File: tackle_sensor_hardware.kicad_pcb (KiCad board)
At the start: 4 copper layers, 45.1 x 57.2 mm, 74 parts, among them J1 Conn_01x02_Male, J2 Conn_01x04_Male, J3 Conn_01x03_Male, J4 Conn_ARM_JTAG_SWD_10, Q1 DMP4051LK3, Q9 NCE0110K, SW1 PTS645SL43SMTR92 LFS, SW2 SW_DPDT_x2, T1 DRQ125-330-R, U1 LIS2DE12, U2 STM32G031Fx, U3 LM3488, U4 LD1117S33TR_SOT223, U5 ULN2003ADR

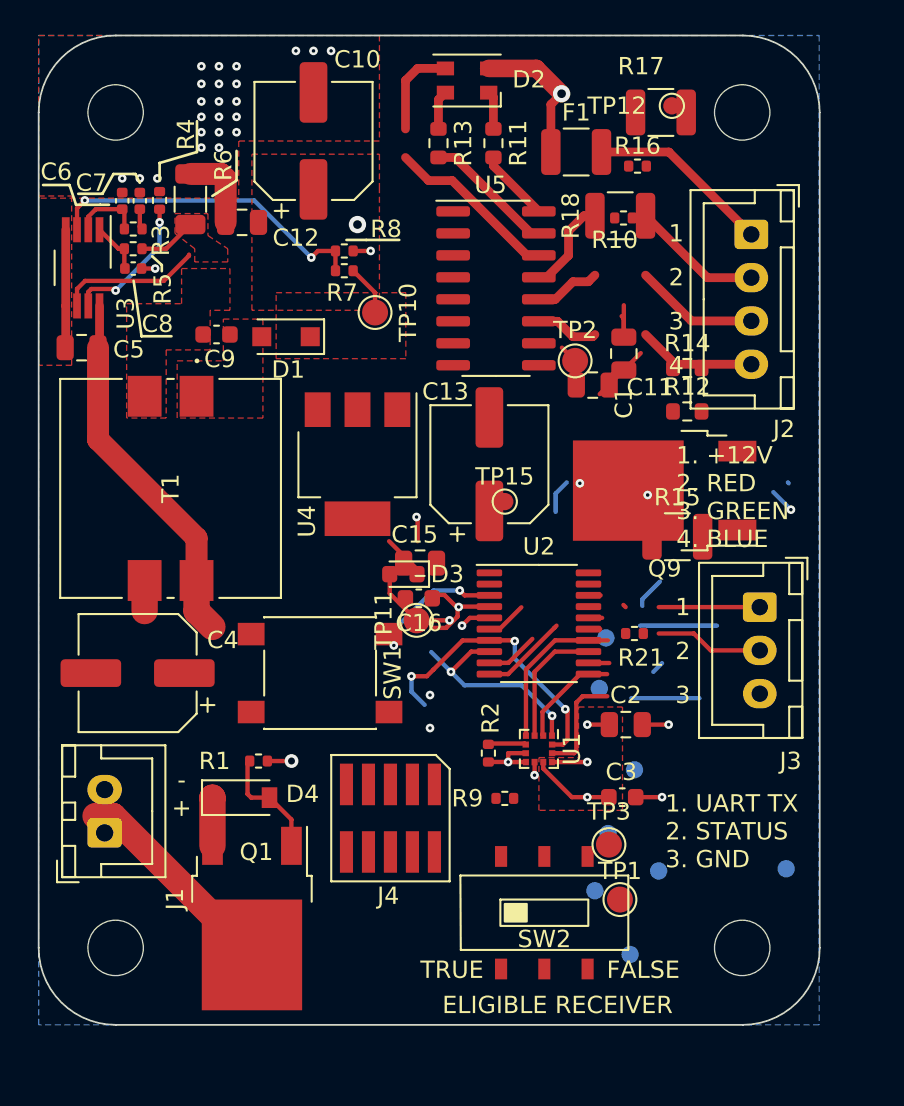
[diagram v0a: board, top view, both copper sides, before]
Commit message: rerouted PCB after changes
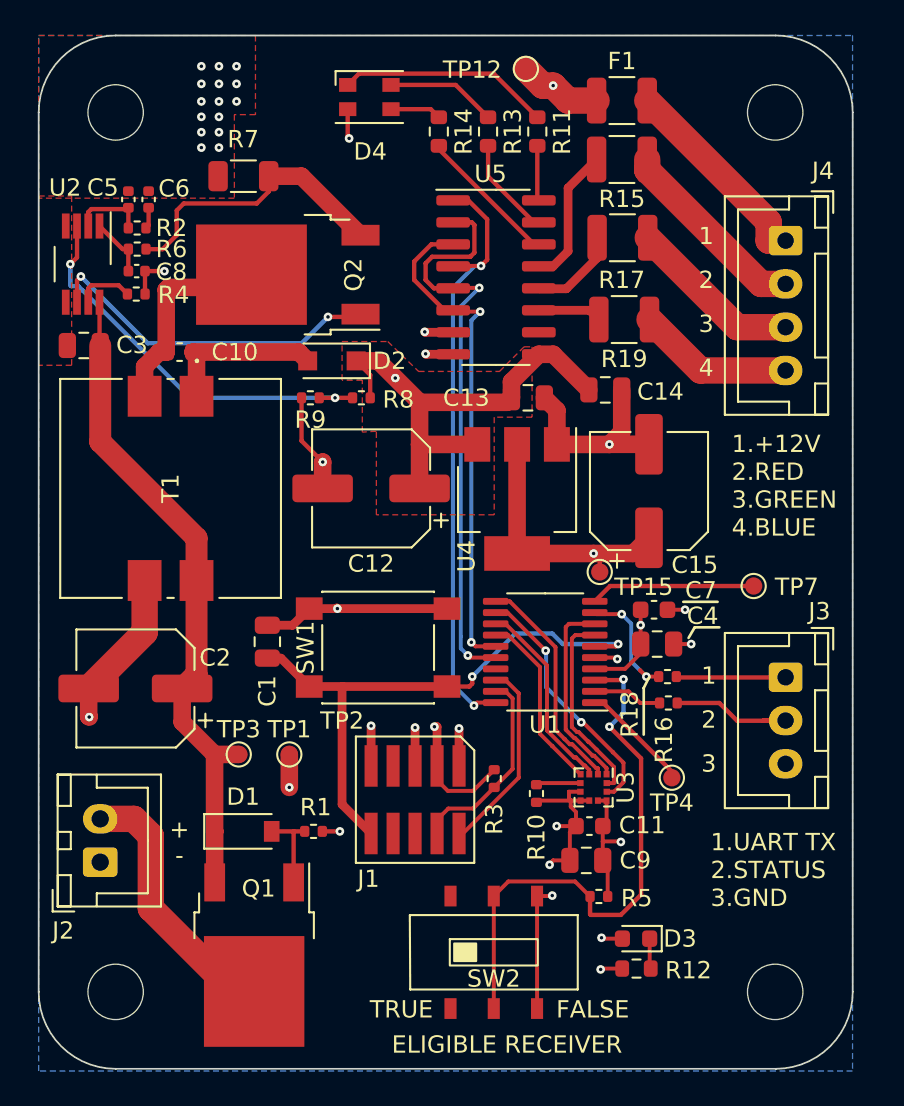
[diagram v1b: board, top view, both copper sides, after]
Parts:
- removed C16: 1uF, 50V, Capacitor_SMD:C_0603_1608Metric
- removed Q9: NCE0110K, Package_TO_SOT_SMD:TO-252-2
- removed R21: 220,1%,63mW, Resistor_SMD:R_0402_1005Metric
- removed TP5: TestPoint, TestPoint:TestPoint_Pad_D1.0mm
- added C14: 100nF, 50V, Capacitor_SMD:C_0805_2012Metric, F.Cu at (153.4, 90.3)
- added Q2: NCE0110K, Package_TO_SOT_SMD:TO-252-2, F.Cu at (135.0, 83.7)
- added R19: 0,0.5W, Resistor_SMD:R_1210_3225Metric, F.Cu at (154.5, 86.3)
- C10: value 22uF, 20V -> 1uF, 50V; footprint Capacitor_SMD:CP_Elec_6.3x5.9 -> Capacitor_SMD:C_0603_1608Metric
- C11: value 100nF, 50V -> 1uF, 50V; footprint Capacitor_SMD:C_0805_2012Metric -> Capacitor_SMD:C_0603_1608Metric
- C12: value 100nF, 50V -> 22uF, 20V; footprint Capacitor_SMD:C_0805_2012Metric -> Capacitor_SMD:CP_Elec_6.3x5.9
- C13, C4: value 10uF, 50V -> 100nF, 50V; footprint Capacitor_SMD:CP_Elec_6.3x5.8 -> Capacitor_SMD:C_0805_2012Metric
- C15, C2: value 100nF, 50V -> 10uF, 50V; footprint Capacitor_SMD:C_0805_2012Metric -> Capacitor_SMD:CP_Elec_6.3x5.8
- C3: value 10u -> 100nF, 50V; footprint Capacitor_SMD:C_0603_1608Metric -> Capacitor_SMD:C_0805_2012Metric
- C5: value 100nF, 50V -> 2200pF,10%,50V; footprint Capacitor_SMD:C_0805_2012Metric -> Capacitor_SMD:C_0402_1005Metric
- C6: value 2200pF,10%,50V -> 0.22uF,10%,35V
- C7: value 0.22uF,10%,35V -> 1uF, 50V; footprint Capacitor_SMD:C_0402_1005Metric -> Capacitor_SMD:C_0603_1608Metric
- C9: value 1uF, 50V -> 100nF, 50V; footprint Capacitor_SMD:C_0603_1608Metric -> Capacitor_SMD:C_0805_2012Metric
- D1: value DSK34 -> BZT52-B15_R1_00001; footprint Diode_SMD:D_SOD-123F -> Diode_SMD:D_SOD-123
- D2: value CLV1A-FKB-CK1VW1DE1BB7C3C3 -> DSK34; footprint LED_SMD:LED_Cree-PLCC4_3.2x2.8mm_CCW -> Diode_SMD:D_SOD-123F
- D4: value BZT52-B15_R1_00001 -> CLV1A-FKB-CK1VW1DE1BB7C3C3; footprint Diode_SMD:D_SOD-123 -> LED_SMD:LED_Cree-PLCC4_3.2x2.8mm_CCW
- J1: value Conn_01x02_Male -> Conn_ARM_JTAG_SWD_10; footprint Connector_JST:JST_XH_B2B-XH-A_1x02_P2.50mm_Vertical -> rfc_footprint_lib:20021121-00010C4LF
- J2: value Conn_01x04_Male -> Conn_01x02_Male; footprint Connector_JST:JST_XH_B4B-XH-A_1x04_P2.50mm_Vertical -> Connector_JST:JST_XH_B2B-XH-A_1x02_P2.50mm_Vertical
- J4: value Conn_ARM_JTAG_SWD_10 -> Conn_01x04_Male; footprint rfc_footprint_lib:20021121-00010C4LF -> Connector_JST:JST_XH_B4B-XH-A_1x04_P2.50mm_Vertical
- R10: value 10k,1%,63mW -> 0,63mW
- R18: value 0,0.5W -> 220,1%,63mW; footprint Resistor_SMD:R_1210_3225Metric -> Resistor_SMD:R_0402_1005Metric
- R2: value 0,63mW -> 634,.1%,63mW
- R3: value 634,.1%,0.1W -> 10k,1%,63mW
- R5: value 100,1%,63mW -> 10k,1%,63mW
- R6: value 25mOhm,1%,500mW -> 100,1%,63mW; footprint Resistor_SMD:R_1206_3216Metric -> Resistor_SMD:R_0402_1005Metric
- R7: value 84.5k,1%,63mW -> 25mOhm,1%,500mW; footprint Resistor_SMD:R_0402_1005Metric -> Resistor_SMD:R_1206_3216Metric
- R8: value 10k,1%,63mW -> 84.5k,1%,63mW
- TP1, TP3: footprint TestPoint:TestPoint_Pad_D1.5mm -> TestPoint:TestPoint_Pad_D1.0mm
- TP10, TP11, TP2: footprint TestPoint:TestPoint_Pad_D1.5mm -> rfc_footprint_lib:test_point
- TP13, TP14, TP6, TP8, TP9: footprint TestPoint:TestPoint_Pad_D1.0mm -> rfc_footprint_lib:test_point; moved to F.Cu
- TP4, TP7: moved to F.Cu
- U1: value LIS2DE12 -> STM32G031Fx; footprint Package_LGA:LGA-12_2x2mm_P0.5mm -> Package_SO:TSSOP-20_4.4x6.5mm_P0.65mm
- U2: value STM32G031Fx -> LM3488; footprint Package_SO:TSSOP-20_4.4x6.5mm_P0.65mm -> Package_SO:VSSOP-8_3.0x3.0mm_P0.65mm
- U3: value LM3488 -> LIS2DE12; footprint Package_SO:VSSOP-8_3.0x3.0mm_P0.65mm -> Package_LGA:LGA-12_2x2mm_P0.5mm
- moved J2 52.2 mm to (124.2, 117.6), turned to 90 degrees
- moved R5 46.1 mm to (153.0, 119.6), turned to 180 degrees
- moved U3 42.1 mm to (152.7, 113.3)
- moved D4 41.1 mm to (139.8, 73.4)
- moved C3 40.6 mm to (123.3, 87.8), turned to 180 degrees
- moved J4 40.4 mm to (163.8, 81.7), turned to -90 degrees
- moved R3 38.0 mm to (147.0, 112.8), turned to -90 degrees
- moved C7 38.0 mm to (156.2, 103.0), turned to 0 degrees
- moved C9 37.1 mm to (152.3, 117.5)
- moved R2 36.5 mm to (126.3, 81.0), turned to 0 degrees
- moved R10 33.6 mm to (149.4, 113.6), turned to -90 degrees
- moved U2 33.5 mm to (123.2, 83.1), turned to -90 degrees
- moved R12 32.3 mm to (155.2, 123.7), turned to 180 degrees
- moved R16 31.1 mm to (157.0, 108.4)
- moved C4 30.1 mm to (156.4, 105.0), turned to 0 degrees
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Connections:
- C10 pad 1: +12V -> Net-(C10-Pad1)
- C10 pad 2: GND -> Net-(C10-Pad2)
- C11 pad 1: +12V -> +3V3
- C13 pad 1: +3V3 -> +12V
- C2 pad 1: +3V3 -> Net-(C2-Pad1)
- C3 pad 1: +3V3 -> Net-(C2-Pad1)
- C4 pad 1: Net-(C4-Pad1) -> +3V3
- C5 pad 1: Net-(C4-Pad1) -> Net-(C5-Pad1)
- C7 pad 1: Net-(C7-Pad1) -> +3V3
- C9 pad 1: Net-(C9-Pad1) -> +3V3
- C9 pad 2: Net-(C9-Pad2) -> GND
- D1 pad 1: +12V -> Net-(C2-Pad1)
- D1 pad 2: Net-(C9-Pad1) -> Net-(D1-Pad2)
- D2 pad 1: Net-(D2-Pad1) -> +12V
- D2 pad 2: +12V -> Net-(C10-Pad1)
- D4 pad 1: Net-(C4-Pad1) -> Net-(D4-Pad1)
- D4 pad 2: Net-(D4-Pad2) -> +12V
- J1 pad 1: GND -> +3V3
- J1 pad 2: Net-(J1-Pad2) -> /SWDIO
- J2 pad 1: Net-(F1-Pad2) -> GND
- J4 pad 1: +3V3 -> Net-(F1-Pad2)
- J4 pad 2: /SWDIO -> Net-(J4-Pad2)
- J4 pad 3: GND -> Net-(J4-Pad3)
- J4 pad 4: /SWCLK -> Net-(J4-Pad4)
- Q1 pad 1: Net-(D4-Pad2) -> Net-(D1-Pad2)
- Q1 pad 2: Net-(J1-Pad2) -> Net-(J2-Pad2)
- Q1 pad 3: Net-(C4-Pad1) -> Net-(C2-Pad1)
- R1 pad 1: Net-(D4-Pad2) -> Net-(D1-Pad2)
- R10 pad 1: Net-(R7-Pad2) -> Net-(R10-Pad1)
- R11 pad 1: Net-(D2-Pad1) -> Net-(D4-Pad1)
- R12 pad 1: Net-(D2-Pad4) -> Net-(D3-Pad1)
- R12 pad 2: Net-(U5-Pad15) -> GND
- R13 pad 1: Net-(D2-Pad3) -> Net-(D4-Pad4)
- R13 pad 2: Net-(U5-Pad14) -> Net-(R13-Pad2)
- R14 pad 1: Net-(D3-Pad1) -> Net-(D4-Pad3)
- R14 pad 2: GND -> Net-(R14-Pad2)
- R15 pad 1: Net-(U5-Pad12) -> Net-(J4-Pad2)
- R15 pad 2: Net-(J2-Pad3) -> Net-(R15-Pad2)
- R16 pad 1: UART_TX -> TACKLE_STATUS
- R16 pad 2: Net-(J3-Pad1) -> Net-(J3-Pad2)
- R17 pad 1: Net-(U5-Pad11) -> Net-(J4-Pad3)
- R17 pad 2: Net-(J2-Pad4) -> Net-(R17-Pad2)
- R18 pad 1: Net-(R18-Pad1) -> UART_TX
- R18 pad 2: Net-(J2-Pad2) -> Net-(J3-Pad1)
- R2 pad 1: Net-(R2-Pad1) -> Net-(C5-Pad1)
- R2 pad 2: GND -> Net-(C6-Pad1)
- R3 pad 1: Net-(C6-Pad1) -> GND
- R3 pad 2: Net-(C7-Pad1) -> /SWCLK
- R5 pad 1: Net-(C8-Pad1) -> +3V3
- R5 pad 2: Net-(Q9-Pad2) -> Net-(R5-Pad2)
- R6 pad 1: Net-(Q9-Pad2) -> Net-(C8-Pad1)
- R6 pad 2: GND -> Net-(Q2-Pad2)
- R7 pad 1: +12V -> Net-(Q2-Pad2)
- R7 pad 2: Net-(R7-Pad2) -> GND
- R8 pad 1: GND -> +12V
- R8 pad 2: /SWCLK -> Net-(R8-Pad2)
- R9 pad 1: +3V3 -> Net-(R8-Pad2)
- R9 pad 2: Net-(SW2-Pad2) -> GND
- SW2 pad 2: Net-(SW2-Pad2) -> Net-(R5-Pad2)
- SW2 pad 5: Net-(SW2-Pad2) -> Net-(R5-Pad2)
- T1 pad 1: Net-(C9-Pad1) -> Net-(C10-Pad1)
- T1 pad 2: Net-(C9-Pad2) -> Net-(C10-Pad2)
- T1 pad 4: Net-(C4-Pad1) -> Net-(C2-Pad1)
- TP10 pad 1: +12V -> /SPI1_MISO
- TP11 pad 1: +3V3 -> /SPI1_SCK
- TP12 pad 1: Net-(TP12-Pad1) -> +12V
- TP13 pad 1: UART_TX -> /ACC_INT1
- TP14 pad 1: UART_RX -> /ACC_INT2
- TP15 pad 1: Net-(TP15-Pad1) -> +3V3
- TP3 pad 1: Net-(C4-Pad1) -> Net-(C2-Pad1)
- TP4 pad 1: /SPI1_NSS -> Net-(TP4-Pad1)
- TP6 pad 1: /SPI1_MISO -> UART_TX
- TP7 pad 1: /SPI1_SCK -> UART_RX
- TP8 pad 1: /ACC_INT1 -> /SPI1_NSS
- TP9 pad 1: /ACC_INT2 -> /SPI1_MOSI
- U1 pad 1: /SPI1_SCK -> Net-(TP4-Pad1)
- U1 pad 10: +3V3 -> UART_RX
- U1 pad 11: /ACC_INT2 -> /SPI1_NSS
- U1 pad 12: /ACC_INT1 -> /ACC_INT2
- U1 pad 2: /SPI1_NSS -> TACKLE_STATUS
- U1 pad 3: /SPI1_MISO -> Net-(R5-Pad2)
- U1 pad 4: /SPI1_MOSI -> +3V3
- U1 pad 5: Net-(R2-Pad1) -> GND
- U1 pad 6: GND -> /RST
- U1 pad 7: GND -> /ACC_INT1
- U1 pad 8: GND -> /SPI1_SCK
- U1 pad 9: +3V3 -> UART_TX
- U2 pad 1: Net-(TP15-Pad1) -> Net-(C8-Pad1)
- U2 pad 2: TACKLE_STATUS -> Net-(C5-Pad1)
- U2 pad 3: Net-(SW2-Pad2) -> Net-(R8-Pad2)
- U2 pad 4: +3V3 -> GND
- U2 pad 6: /RST -> Net-(Q2-Pad1)
- U2 pad 7: /ACC_INT1 -> Net-(R4-Pad1)
- U2 pad 8: /SPI1_SCK -> Net-(C2-Pad1)
- U3 pad 1: Net-(C8-Pad1) -> /SPI1_SCK
- U3 pad 2: Net-(C6-Pad1) -> /SPI1_NSS
- U3 pad 3: Net-(R7-Pad2) -> /SPI1_MISO
- U3 pad 4: GND -> /SPI1_MOSI
- U3 pad 5: GND -> Net-(R10-Pad1)
- U3 pad 6: Net-(Q9-Pad1) -> GND
- U3 pad 7: Net-(R4-Pad1) -> GND
- U3 pad 8: Net-(C4-Pad1) -> GND
- U5 pad 11: Net-(U5-Pad11) -> Net-(R19-Pad2)
- U5 pad 12: Net-(U5-Pad12) -> Net-(R17-Pad2)
- U5 pad 13: Net-(R18-Pad1) -> Net-(R15-Pad2)
- U5 pad 14: Net-(U5-Pad14) -> Net-(R14-Pad2)
- U5 pad 15: Net-(U5-Pad15) -> Net-(R13-Pad2)
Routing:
- net +12V: track 11.4 -> 63.8 mm, vias 2 -> 3
- net GND: track 29.4 -> 80.9 mm, vias 32 -> 34
- net Net-(C2-Pad1): track 0.00 -> 38.5 mm
- net R_PWM: track 0.00 -> 36.0 mm, vias 0 -> 2
- net G_PWM: track 0.79 -> 33.7 mm, vias 0 -> 2
- net Net-(R5-Pad2): track 0.00 -> 32.5 mm, vias 0 -> 2
- net B_PWM: track 0.67 -> 29.1 mm, vias 0 -> 2
- net /RST: track 6.80 -> 33.3 mm, vias 0 -> 2
- net Net-(C4-Pad1): track 24.2 -> 0.00 mm
- net Net-(R8-Pad2): track 0.00 -> 23.5 mm, vias 0 -> 2
- net Net-(Q2-Pad1): track 0.00 -> 20.3 mm, vias 0 -> 2
- net Net-(R7-Pad2): track 19.0 -> 0.00 mm, vias 2 -> 0
- net Net-(Q2-Pad2): track 0.00 -> 16.9 mm
- net Net-(C10-Pad2): track 0.00 -> 13.0 mm
- net +3V3: track 19.1 -> 31.7 mm
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- removed copper zone on F.Cu, net +3V3
- removed copper zone on F.Cu, net Net-(C9-Pad1)
- removed copper zone on F.Cu, net Net-(C9-Pad2)
- removed copper zone on F.Cu, net Net-(Q9-Pad1)
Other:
- board size 45.1 x 57.2 mm -> 47 x 59.7 mm
- board text added: "1.+12V 2.RED 3.GREEN 4.BLUE"
- board text added: "1.UART TX 2.STATUS 3.GND"
- board text added: "Robotic Football Tackle Sensor V0.2 10/23/2022"
- board text removed: "1. +12V 2. RED 3. GREEN 4. BLUE"
- board text removed: "1. UART TX 2. STATUS 3. GND"
- board text removed: "Robotic Football Tackle Sensor V0.0 4/18/2022"

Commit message: adding release v0.1
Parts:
- removed the G*** at (143.4, 95.5) (x2)
- added G***: LOGO, rfc_footprint_lib:new_logo_mask, B.Cu at (145.2, 96.3)
- added G***: LOGO, rfc_footprint_lib:new_logo_silk, B.Cu at (145.2, 96.3)
- moved C10 1.27 mm to (127.5, 87.9)
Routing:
- net Net-(C10-Pad1): track 9.47 -> 11.1 mm
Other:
- board text added: "Tackle Sensor V0.1 10/24/2022"
- board text removed: "Robotic Football Tackle Sensor V0.2 10/23/2022"

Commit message: - updates for release v0.1
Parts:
- removed TP6: TestPoint, rfc_footprint_lib:test_point
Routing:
- net /SWDIO: track 11.3 -> 12.4 mm
- net R_PWM: track 36.0 -> 35.0 mm
- net Net-(C10-Pad2): track 12.8 -> 12.0 mm
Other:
- board text added: "Tackle Sensor V0.1 12/1/2022"
- board text removed: "Tackle Sensor V0.1 10/24/2022"

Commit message: - add reference PDFs and dimensions to the layout
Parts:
- moved C14 39.5 mm to (145.4, 51.6)
- moved C15 39.5 mm to (147.9, 57.4)
- moved D1 39.5 mm to (124.5, 77.1)
- moved F1 39.5 mm to (146.4, 34.9)
- moved J1 39.5 mm to (134.4, 75.3)
- moved R10 39.5 mm to (141.4, 74.9)
- moved R12 39.5 mm to (147.2, 85.0)
- moved R14 39.5 mm to (135.8, 36.7)
- moved R15 39.5 mm to (146.4, 38.3)
- moved R3 39.5 mm to (139.0, 74.0)
- moved R5 39.5 mm to (145.0, 80.8)
- moved R9 39.5 mm to (128.4, 52.0)
- moved SW1 39.5 mm to (132.3, 66.5)
- moved TP12 39.5 mm to (140.8, 33.0)
- moved TP13 39.5 mm to (144.4, 71.9)
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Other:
- board text added: "Electrical Connector Details Power Connector - J2 Pin 1 - GND Pin 2 - V+ (10V to 30V) Status Connector - J3 (Optional) Pin 1 - UART TX (115200 bps, 8N1, 3.3V Logic Output) Pin 2 - STATUS (3.3V Logic Output) Pin 3 - GND LED Connector - J4 (Common Anode RGB LED) Pin 1 - +12V Pin 2 - RED Pin 3 - GREEN Pin 4 - BLUE"

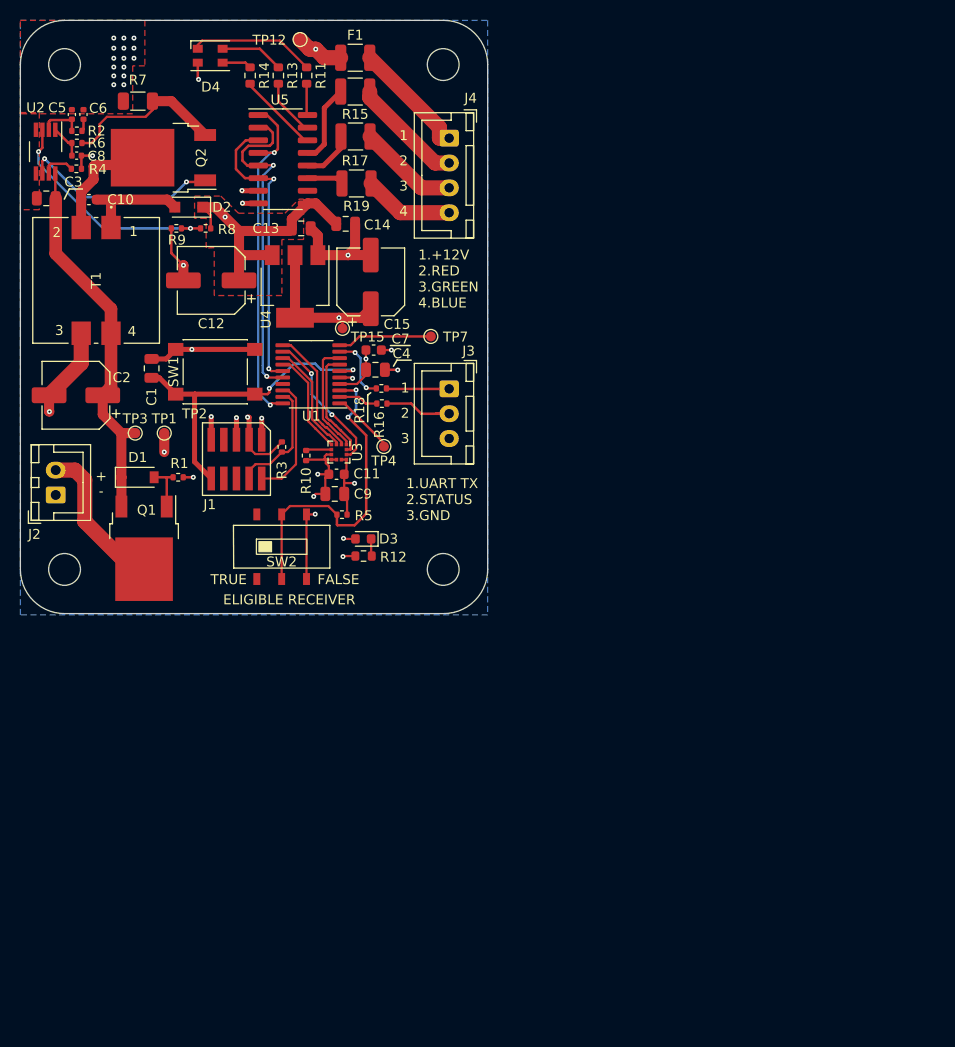
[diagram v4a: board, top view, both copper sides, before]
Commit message: - change page size to legal
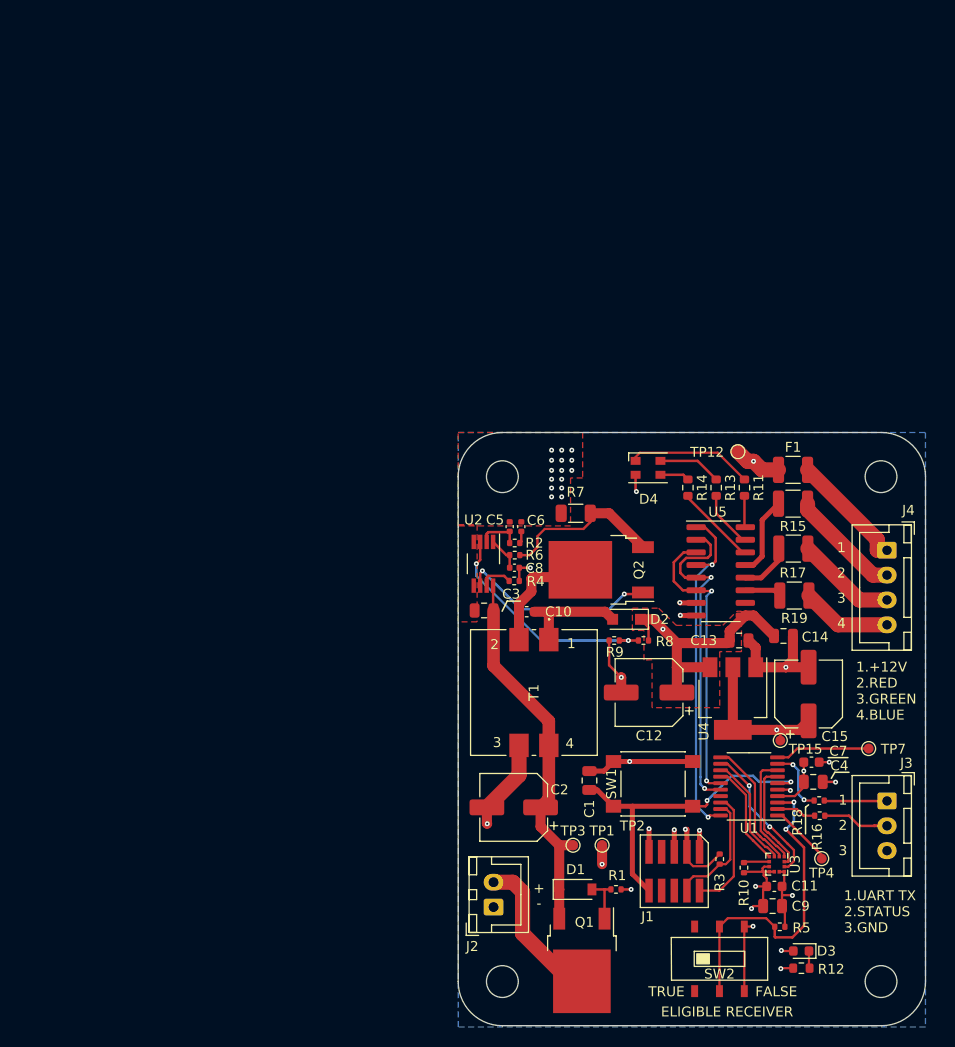
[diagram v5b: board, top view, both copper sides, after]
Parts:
- moved C15 60.5 mm to (192.0, 98.9)
- moved J1 60.5 mm to (178.5, 116.7)
- moved R14 60.5 mm to (179.8, 78.1)
- moved TP13 60.5 mm to (188.5, 113.4)
- moved C1 60.5 mm to (169.9, 107.6)
- moved C14 60.5 mm to (189.5, 93.1)
- moved H3 60.5 mm to (161.2, 127.8)
- moved R12 60.5 mm to (191.3, 126.5)
- moved R2 60.5 mm to (162.4, 83.7)
- moved R5 60.5 mm to (189.1, 122.3)
- moved R9 60.5 mm to (172.4, 93.5)
- moved SW1 60.5 mm to (176.3, 107.9)
- moved T1 60.5 mm to (164.4, 98.7)
- moved U3 60.5 mm to (188.8, 116.0)
- moved C10 60.5 mm to (163.6, 90.6)
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
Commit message: - added additional notes to the reference_sheet and the schematic sheet
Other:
- board text added: "Electrical Connector Details Power Connector - J2 Mating Connector Housing: XHP-2 Mating Connector Pins: (see below) - Pin 1 - GND - Pin 2 - V+ (10V to 30V) Status Connector - J3 (Optional) Mating Connector Housing: XHP-3 Mating Connector Pins: (see below) - Pin 1 - UART TX (115200 bps, 8N1, 3.3V Logic Output) - Pin 2 - STATUS (3.3V Logic Output) - Pin 3 - GND LED Connector - J4 (Common Anode RGB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"
- board text removed: "Electrical Connector Details Power Connector - J2 Pin 1 - GND Pin 2 - V+ (10V to 30V) Status Connector - J3 (Optional) Pin 1 - UART TX (115200 bps, 8N1, 3.3V Logic Output) Pin 2 - STATUS (3.3V Logic Output) Pin 3 - GND LED Connector - J4 (Common Anode RGB LED) Pin 1 - +12V Pin 2 - RED Pin 3 - GREEN Pin 4 - BLUE"
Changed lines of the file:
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@@
   (gr_line (start 191.6861 112.9682) (end 191.6861 110.2758) (layer "F.SilkS") (width 0.155))
   (gr_line (start 195.9533 105.2974) (end 193.9721 105.2974) (layer "F.SilkS") (width 0.155))
-  (gr_rect (start 15.24 15.24) (end 84.455 19.812) (layer "Cmts.User") (width 0.155) (fill none))
-  (gr_rect (start 15.24 15.24) (end 84.455 62.103) (layer "Cmts.User") (width 0.155) (fill none))
+  (gr_rect (start 15.24 15.24) (end 103.632 20.066) (layer "Cmts.User") (width 0.155) (fill none))
+  (gr_rect (start 15.24 15.24) (end 103.632 99.06) (layer "Cmts.User") (width 0.155) (fill none))
   (gr_line (start 203.757602 77.0272) (end 203.757602 127.8272) (layer "Edge.Cuts") (width 0.1))
   (gr_arc (start 156.7357 77.0272) (mid 158.03761 73.88411) (end 161.1807 72.5822) (layer "Edge.Cuts") (width 0.1))
@@
     (effects (font (size 1 1) (thickness 0.15)))
   )
-  (gr_text "Electrical Connector Details\n\nPower Connector - J2\nPin 1 - GND \nPin 2 - V+ (10V to 30V)\n\nStatus Connector - J3 \n(Optional)\nPin 1 - UART TX (115200 bps, 8N1, 3.3V Logic Output)\nPin 2 - STATUS (3.3V Logic Output)\nPin 3 - GND\n\nLED Connector - J4\n(Common Anode RGB LED)\nPin 1 - +12V\nPin 2 - RED\nPin 3 - GREEN\nPin 4 - BLUE" (at 16.764 38.481) (layer "Cmts.User")
+  (gr_text "Electrical Connector Details\n\nPower Connector - J2\nMating Connector Housing: XHP-2\nMating Connector Pins: (see below)\n- Pin 1 - GND \n- Pin 2 - V+ (10V to 30V)\n\nStatus Connector - J3 (Optional)\nMating Connector Housing: XHP-3\nMating Connector Pins: (see below)\n- Pin 1 - UART TX (115200 bps, 8N1, 3.3V Logic Output)\n- Pin 2 - STATUS (3.3V Logic Output)\n- Pin 3 - GND\n\nLED Connector - J4\n(Common Anode RGB LED)\nMating Connector Housing: XHP-4\nMating Connector Pins: (see below)\n- Pin 1 - +12V\n- Pin 2 - RED\n- Pin 3 - GREEN\n- Pin 4 - BLUE\n\nAll connector housings in this design \n	use the same style of crimp terminals. \nAn exammple part number for 22-26 AWG wire is below.\n	Mating crimp terminals: SXH-001T-P0.6N (example)\nThe recommended path is to used precrimped jumpers\n	for high-quality connections suchs as ASXHSXH22K305.\nThese cables can be purchased as complete\n	assemblies from places like Amazon. <https://a.co/d/8tT1Qsl>" (at 16.002 55.88) (layer "Cmts.User")
     (effects (font (size 1.524 1.524) (thickness 0.3048)) (justify left))
   )
